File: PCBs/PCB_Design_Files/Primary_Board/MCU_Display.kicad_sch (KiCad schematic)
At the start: 0 parts

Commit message: AFE layout, oled+esp libraries
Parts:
- added U5: MOUDLE-SEEEDUINO-XIAO-ESP32C3, Project Footprints:XIAO_ESP32S3_MODULE, symbol project_symbols:MOUDLE-SEEEDUINO-XIAO-ESP32C3
- added U6: DM-OLED096-636, Project Footprints:OLED096-636, symbol project_symbols:DM-OLED096-636

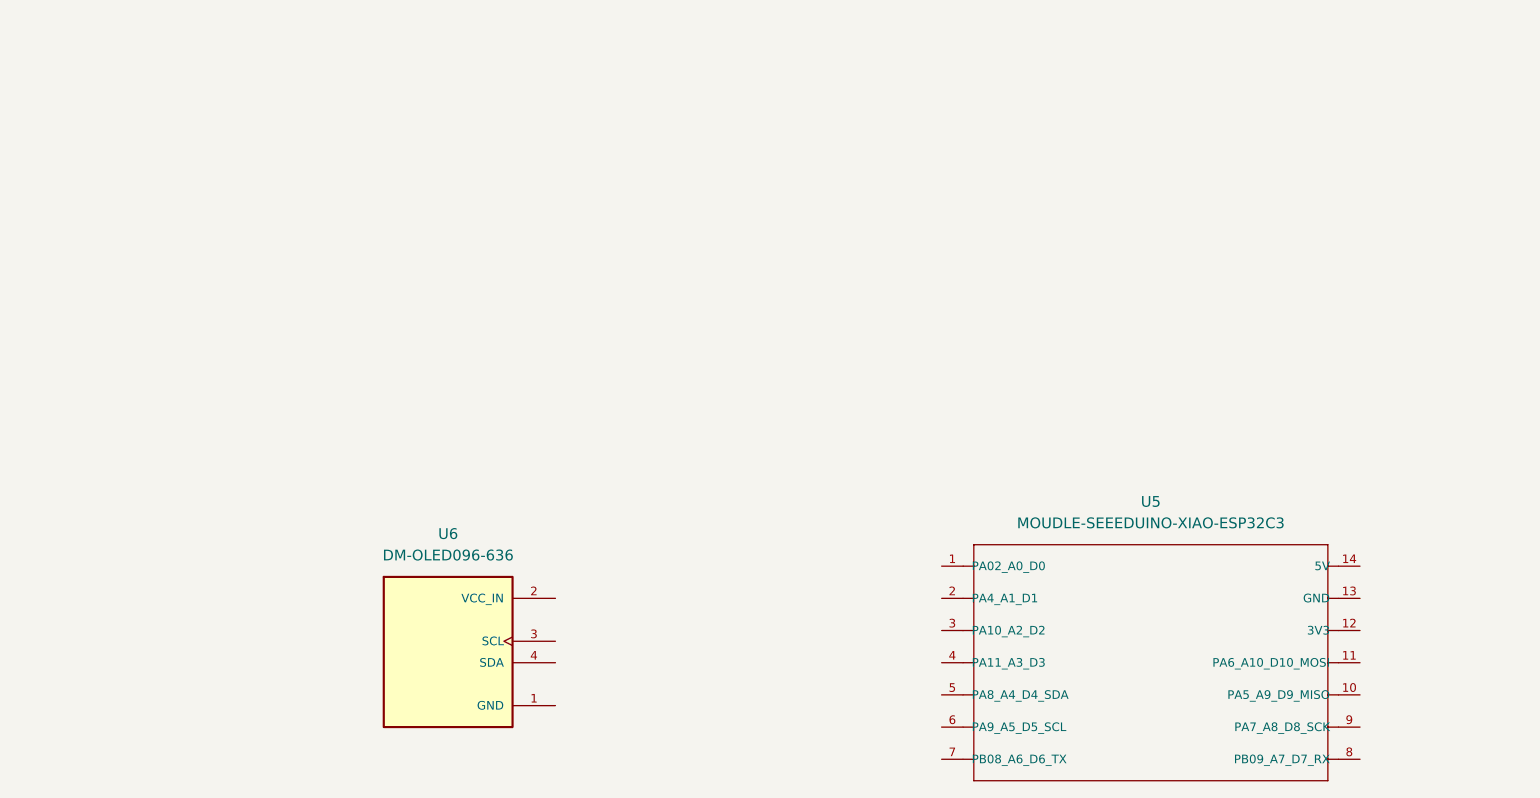
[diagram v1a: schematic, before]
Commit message: Added Voltage Search DAC
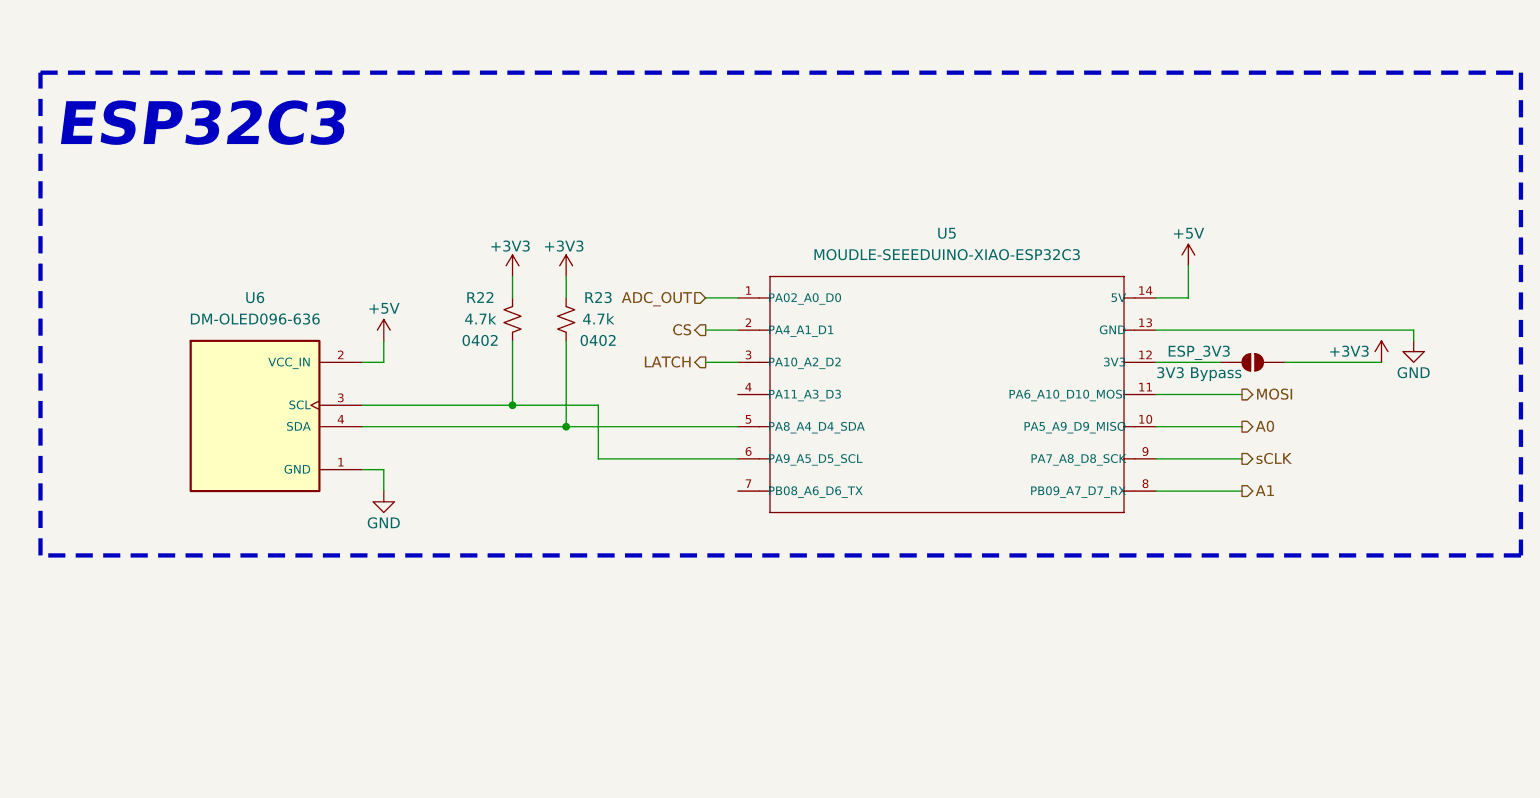
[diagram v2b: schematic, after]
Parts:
- added ESP_3V3: 3V3 Bypass, Jumper:SolderJumper-2_P1.3mm_Open_Pad1.0x1.5mm, symbol Jumper:SolderJumper_2_Open
- added R22, R23: 4.7k, Resistor_SMD:R_0402_1005Metric, symbol Device:R_Small_US
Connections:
- net ADC_OUT: now reaches U5.1 (PA02_A0_D0)
- net A0: now reaches U5.10 (PA5_A9_D9_MISO)
- net MOSI: now reaches U5.11 (PA6_A10_D10_MOSI)
- net at U5.12 (3V3): now also ESP_3V3.1 (A)
- net GND: now reaches U5.13 (GND)
- net GND: now also U6.1 (GND)
- net +5V: now reaches U5.14 (5V)
- net +5V: now also U6.2 (VCC_IN)
- net CS: now reaches U5.2 (PA4_A1_D1)
- net LATCH: now reaches U5.3 (PA10_A2_D2)
- net at U5.5 (PA8_A4_D4_SDA): now also U6.4 (SDA), R23.1
- net at U5.6 (PA9_A5_D5_SCL): now also U6.3 (SCL), R22.1
- net A1: now reaches U5.8 (PB09_A7_D7_RX)
- net sCLK: now reaches U5.9 (PA7_A8_D8_SCK)
- new net +3V3: ESP_3V3.2 (B), R22.2, R23.2
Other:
- note added: "ESP32C3"
- moved on the sheet: U5, U6

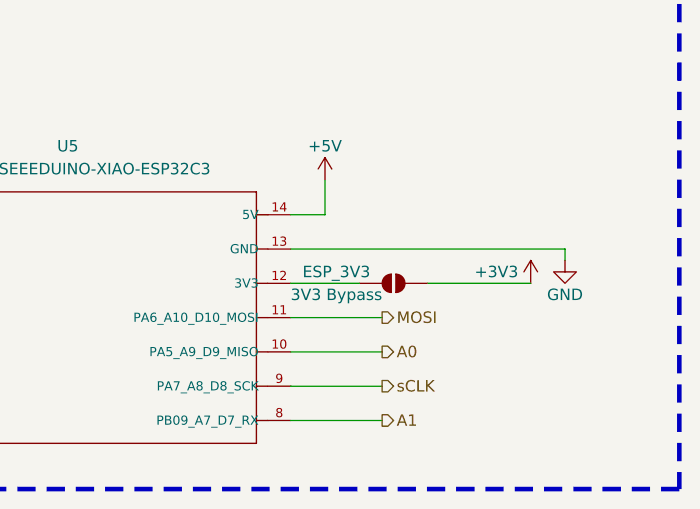
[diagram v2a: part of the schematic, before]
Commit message: schematic update
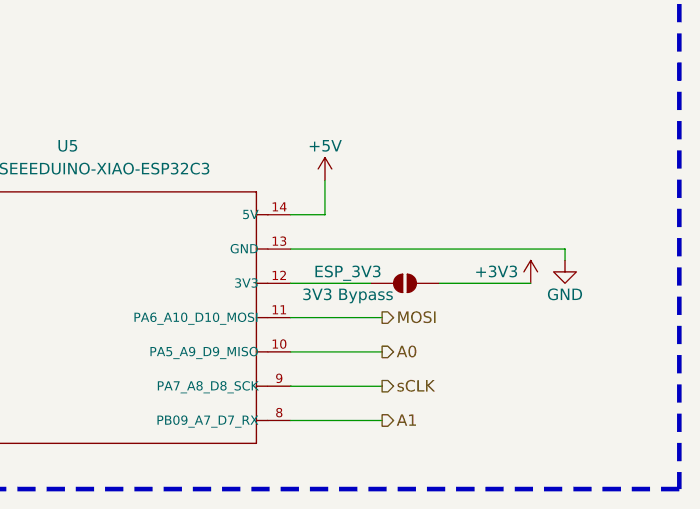
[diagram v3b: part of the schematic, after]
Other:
- moved on the sheet: ESP_3V3
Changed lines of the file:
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@@
 	(wire
 		(pts
-			(xy 165.1 57.15) (xy 176.53 57.15)
+			(xy 166.37 57.15) (xy 176.53 57.15)
 		)
 		(stroke
@@
 	(wire
 		(pts
-			(xy 149.86 57.15) (xy 157.48 57.15)
+			(xy 149.86 57.15) (xy 158.75 57.15)
 		)
 		(stroke
@@
 	(symbol
 		(lib_id "Jumper:SolderJumper_2_Open")
-		(at 161.29 57.15 0)
+		(at 162.56 57.15 0)
 		(unit 1)
 		(exclude_from_sim no)
@@
 		(dnp no)
 		(property "Reference" "ESP_3V3"
-			(at 154.94 55.88 0)
+			(at 156.21 55.88 0)
 			(effects
 				(font
@@
 		)
 		(property "Value" "3V3 Bypass"
-			(at 154.94 58.42 0)
+			(at 156.21 58.42 0)
 			(effects
 				(font
@@
 		)
 		(property "Footprint" "Jumper:SolderJumper-2_P1.3mm_Open_Pad1.0x1.5mm"
-			(at 161.29 57.15 0)
+			(at 162.56 57.15 0)
 			(effects
 				(font
@@
 		)
 		(property "Datasheet" "~"
-			(at 161.29 57.15 0)
+			(at 162.56 57.15 0)
 			(effects
 				(font
@@
 		)
 		(property "Description" "Solder Jumper, 2-pole, open"
-			(at 161.29 57.15 0)
-			(effects
-				(font
+			(at 162.56 57.15 0)
+			(effects
+				(font

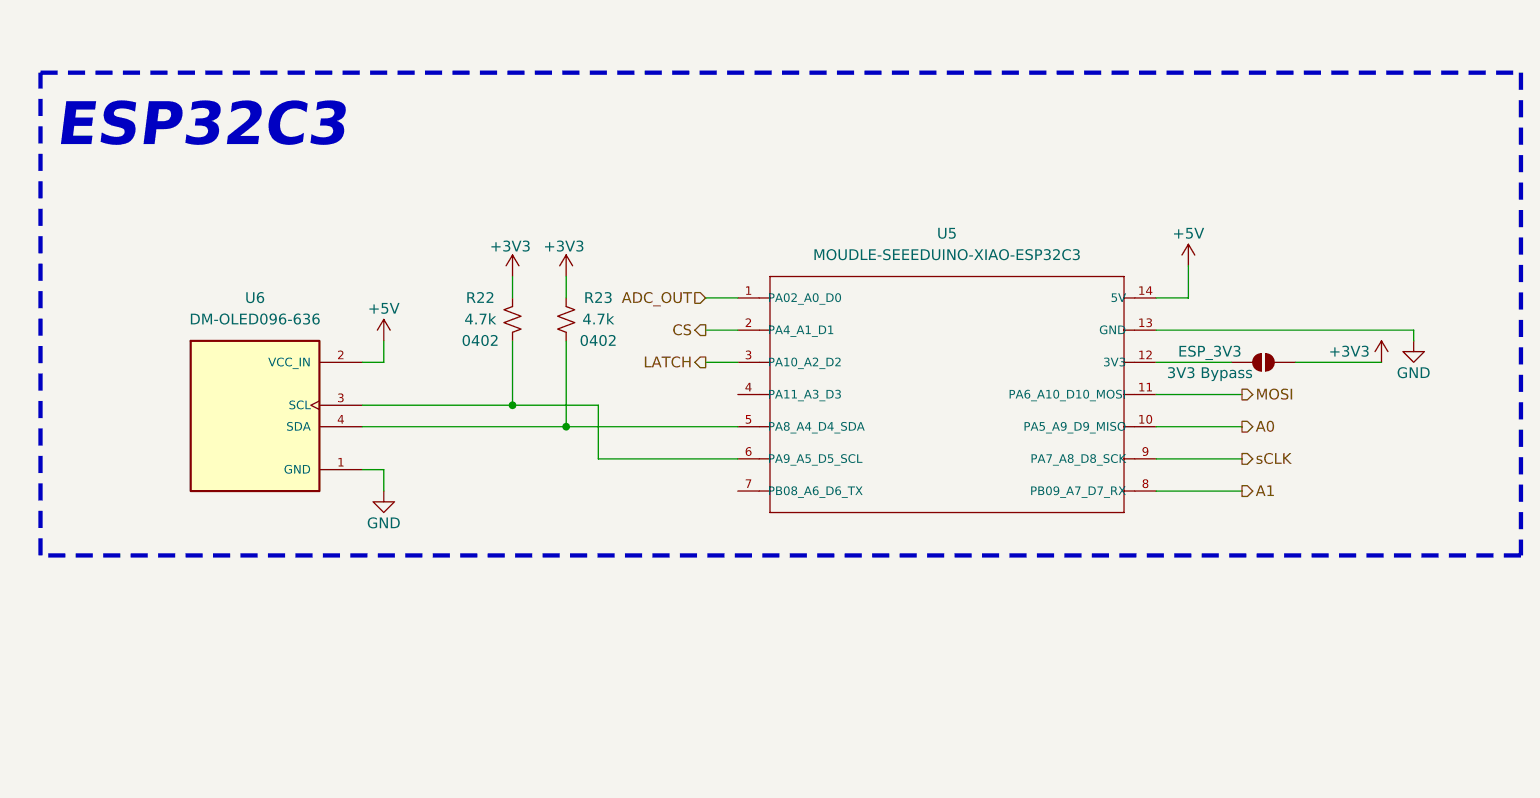
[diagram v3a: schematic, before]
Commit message: updated esp library, primary board connector
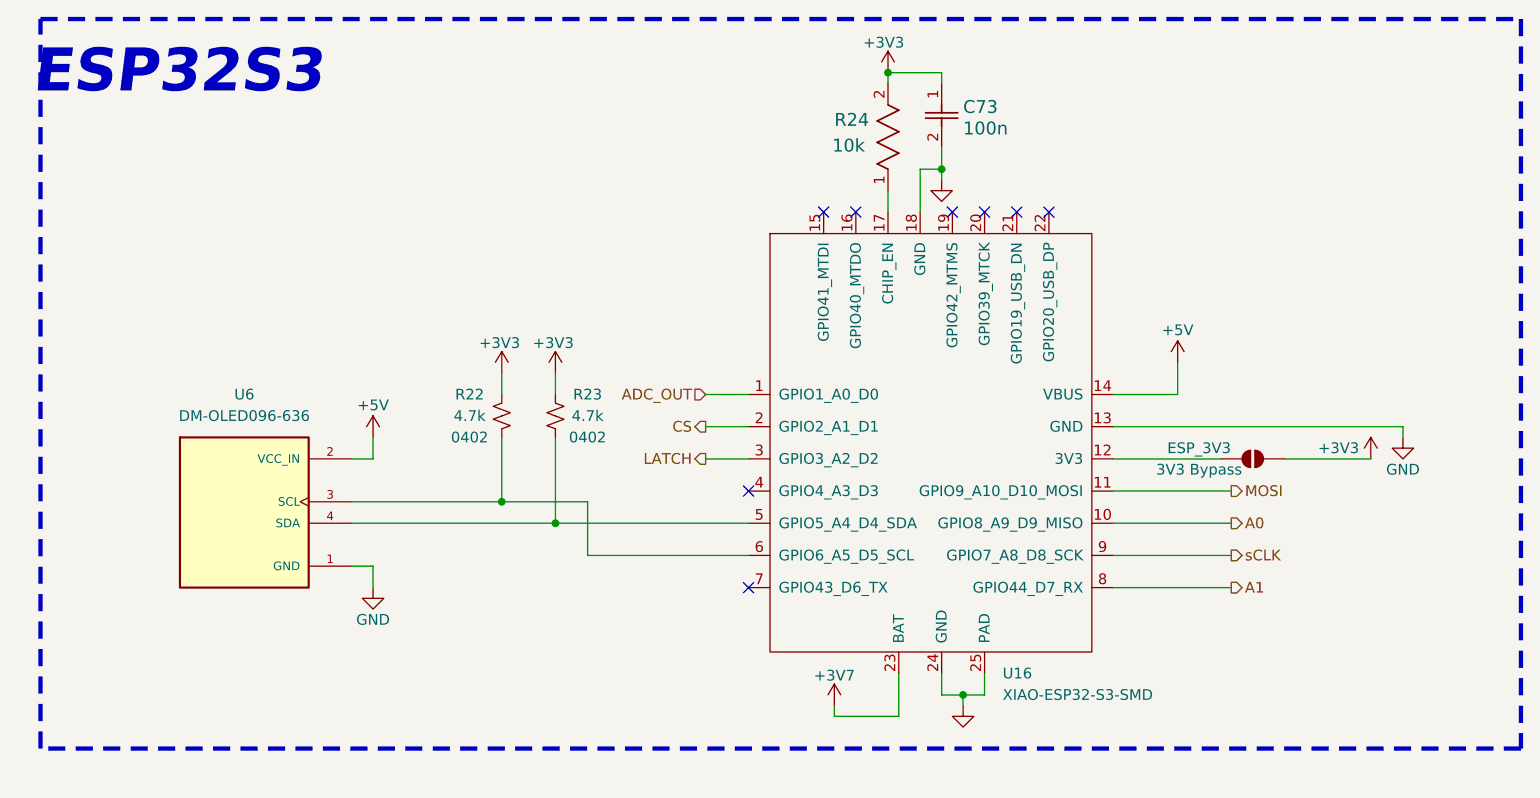
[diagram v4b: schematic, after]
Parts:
- removed U5: MOUDLE-SEEEDUINO-XIAO-ESP32C3, Project Footprints:XIAO_ESP32S3_MODULE, symbol project_symbols:MOUDLE-SEEEDUINO-XIAO-ESP32C3
- added C73: 100n, Project Footprints:0603_capacitor, symbol project_symbols:0603_capacitor
- added R24: 10k, Project Footprints:0603_resistor, symbol project_symbols:0603_resistor
- added U16: XIAO-ESP32-S3-SMD, Project Footprints:XIAO-ESP32-S3-SMD, symbol seed_esp_sym:XIAO-ESP32-S3-SMD
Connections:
- net +3V3: now also C73.1, R24.2
- net +5V: now also U16.14 (VBUS)
- net A0: now also U16.10 (GPIO8_A9_D9_MISO)
- net A1: now also U16.8 (GPIO44_D7_RX)
- net ADC_OUT: now also U16.1 (GPIO1_A0_D0)
- net CS: now also U16.2 (GPIO2_A1_D1)
- net GND: now also C73.2, U16.13 (GND), U16.18 (GND), U16.24 (GND), U16.25 (PAD)
- net LATCH: now also U16.3 (GPIO3_A2_D2)
- net MOSI: now also U16.11 (GPIO9_A10_D10_MOSI)
- net sCLK: now also U16.9 (GPIO7_A8_D8_SCK)
- net at R22.1, U6.3 (SCL): now also U16.6 (GPIO6_A5_D5_SCL)
- net at ESP_3V3.1 (A): now also U16.12 (3V3)
- net at R23.1, U6.4 (SDA): now also U16.5 (GPIO5_A4_D4_SDA)
- new net: R24.1, U16.17 (CHIP_EN)
- new net +3V7: U16.23 (BAT)
- no-connect marks 0 -> 8
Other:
- note added: "ESP32S3"
- note removed: "ESP32C3"
- moved on the sheet: ESP_3V3, R22, R23, U6

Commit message: updated mcu pins
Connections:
- net +5V: no longer U16.14 (VBUS)
- no-connect marks 8 -> 9
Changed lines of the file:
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@@
+	)
+	(no_connect
+		(at 144.78 60.96)
 	)
 	(no_connect
@@
 	(wire
 		(pts
-			(xy 144.78 60.96) (xy 152.4 60.96)
-		)
-		(stroke
-			(width 0)
-			(type default)
-		)
-	)
-	(wire
-		(pts
 			(xy 82.55 73.66) (xy 82.55 80.01)
 		)
@@
 		(pts
 			(xy 124.46 96.52) (xy 127 96.52)
-		)
-		(stroke
-			(width 0)
-			(type default)
-		)
-	)
-	(wire
-		(pts
-			(xy 152.4 57.15) (xy 152.4 60.96)
 		)
 		(stroke
@@
 		)
 	)
+	(hierarchical_label "PWM_IR"
+		(shape output)
+		(at 154.94 45.72 0)
+		(effects
+			(font
+				(size 1.27 1.27)
+			)
+			(justify left)
+		)
+	)
 	(hierarchical_label "sCLK"
 		(shape output)
@@
 		)
 	)
+	(hierarchical_label "OP_CTRL"
+		(shape output)
+		(at 154.94 50.8 0)
+		(effects
+			(font
+				(size 1.27 1.27)
+			)
+			(justify left)
+		)
+	)
 	(hierarchical_label "ADC_OUT"
 		(shape input)
@@
 		(shape output)
 		(at 158.75 83.82 0)
+		(effects
+			(font
+				(size 1.27 1.27)
+			)
+			(justify left)
+		)
+	)
+	(hierarchical_label "PWM_Red"
+		(shape output)
+		(at 154.94 40.64 0)
 		(effects
 			(font
@@
 					(unit 1)
 				)
-			)
-		)
-	)
-	(symbol
-		(lib_id "power:VCC")
-		(at 152.4 57.15 0)
-		(unit 1)
-		(exclude_from_sim no)
-		(in_bom yes)
-		(on_board yes)
-		(dnp no)
-		(property "Reference" "#PWR084"
-			(at 152.4 60.96 0)
-			(effects
-				(font
-					(size 1.27 1.27)
-				)
-				(hide yes)
-			)
-		)
-		(property "Value" "+5V"
-			(at 152.4 53.34 0)
-			(effects
-				(font
-					(size 1.27 1.27)
-				)
-			)
-		)
-		(property "Footprint" ""
-			(at 152.4 57.15 0)
-			(effects
-				(font
-					(size 1.27 1.27)
-				)
-				(hide yes)
-			)
-		)
-		(property "Datasheet" ""
-			(at 152.4 57.15 0)
-			(effects
-				(font
-					(size 1.27 1.27)
-				)
-				(hide yes)
-			)
-		)
-		(property "Description" "Power symbol creates a global label with name \"VCC\""
-			(at 152.4 57.15 0)
-			(effects
-				(font
-					(size 1.27 1.27)
-				)
-				(hide yes)
-			)
-		)
-		(pin "1"
-		)
-		(instances
-			(project "Primary_Board"
-				(path "/8c3d01e8-a984-4e4e-9220-7d351336a99b/c9d7a52b-c624-454d-af83-5076e9ccc3d1"
-					(reference "#PWR084")
-					(unit 1)
-				)

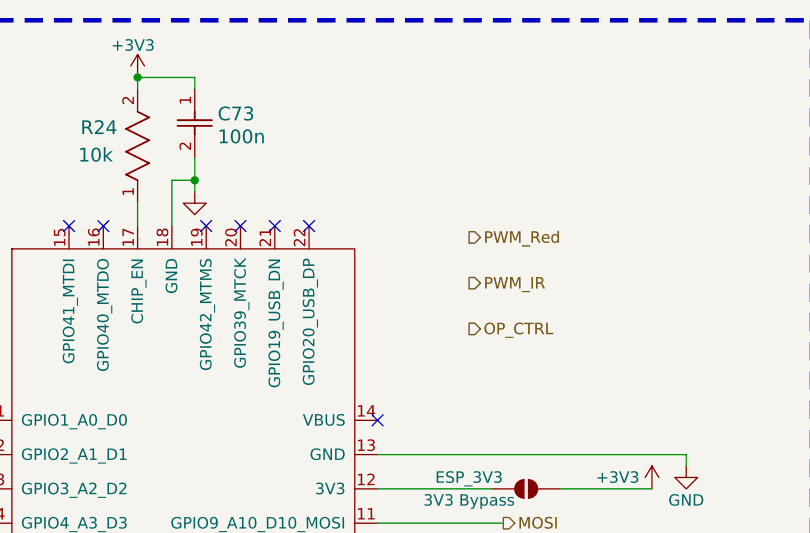
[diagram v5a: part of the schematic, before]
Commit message: routed LED driver gpio on primary board
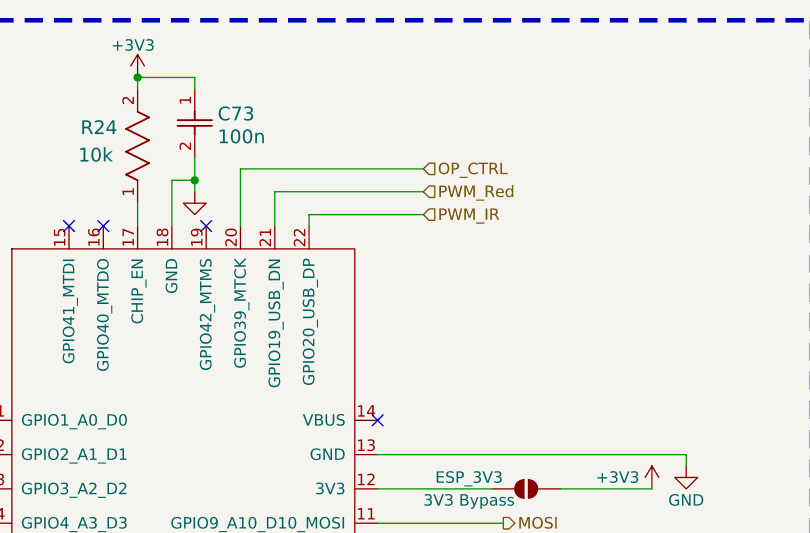
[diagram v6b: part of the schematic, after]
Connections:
- net OP_CTRL: now also U16.20 (GPIO39_MTCK)
- net PWM_IR: now also U16.22 (GPIO20_USB_DP)
- net PWM_Red: now also U16.21 (GPIO19_USB_DN)
- no-connect marks 9 -> 6
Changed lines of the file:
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@@
-	)
-	(no_connect
-		(at 137.16 39.37)
 	)
 	(no_connect
@@
 	)
 	(no_connect
-		(at 129.54 39.37)
-	)
-	(no_connect
 		(at 144.78 60.96)
 	)
@@
 		(at 114.3 39.37)
 	)
-	(no_connect
-		(at 133.35 39.37)
-	)
 	(wire
 		(pts
@@
 	(wire
 		(pts
+			(xy 129.54 33.02) (xy 149.86 33.02)
+		)
+		(stroke
+			(width 0)
+			(type default)
+		)
+	)
+	(wire
+		(pts
 			(xy 72.39 58.42) (xy 72.39 60.96)
 		)
@@
 	(wire
 		(pts
+			(xy 137.16 38.1) (xy 149.86 38.1)
+		)
+		(stroke
+			(width 0)
+			(type default)
+		)
+	)
+	(wire
+		(pts
 			(xy 54.61 76.2) (xy 78.74 76.2)
 		)
@@
 	(wire
 		(pts
+			(xy 137.16 39.37) (xy 137.16 38.1)
+		)
+		(stroke
+			(width 0)
+			(type default)
+		)
+	)
+	(wire
+		(pts
 			(xy 72.39 73.66) (xy 82.55 73.66)
 		)
@@
 	(wire
 		(pts
+			(xy 133.35 35.56) (xy 149.86 35.56)
+		)
+		(stroke
+			(width 0)
+			(type default)
+		)
+	)
+	(wire
+		(pts
 			(xy 54.61 73.66) (xy 72.39 73.66)
 		)
@@
 	(wire
 		(pts
+			(xy 129.54 39.37) (xy 129.54 33.02)
+		)
+		(stroke
+			(width 0)
+			(type default)
+		)
+	)
+	(wire
+		(pts
 			(xy 127 97.79) (xy 127 96.52)
 		)
@@
 		(pts
 			(xy 144.78 83.82) (xy 158.75 83.82)
+		)
+		(stroke
+			(width 0)
+			(type default)
+		)
+	)
+	(wire
+		(pts
+			(xy 133.35 39.37) (xy 133.35 35.56)
 		)
 		(stroke
@@
 	)
 	(hierarchical_label "PWM_IR"
-		(shape output)
-		(at 154.94 45.72 0)
+		(shape input)
+		(at 149.86 38.1 0)
 		(effects
 			(font
@@
 	)
 	(hierarchical_label "OP_CTRL"
-		(shape output)
-		(at 154.94 50.8 0)
+		(shape input)
+		(at 149.86 33.02 0)
 		(effects
 			(font
@@
 	)
 	(hierarchical_label "PWM_Red"
-		(shape output)
-		(at 154.94 40.64 0)
-		(effects
-			(font
+		(shape input)
+		(at 149.86 35.56 0)
+		(effects
+			(font
